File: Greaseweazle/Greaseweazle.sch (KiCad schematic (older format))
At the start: 16 parts, among them J1 FDC_PC, J2 PWR_EXT1, J3 PWR_DRV, J4 PWR_EXT2, J5 USB_TTL, J6 FDC_Amstrad, M1 Mounting, M2 Mounting, M3 Mounting, M4 Mounting

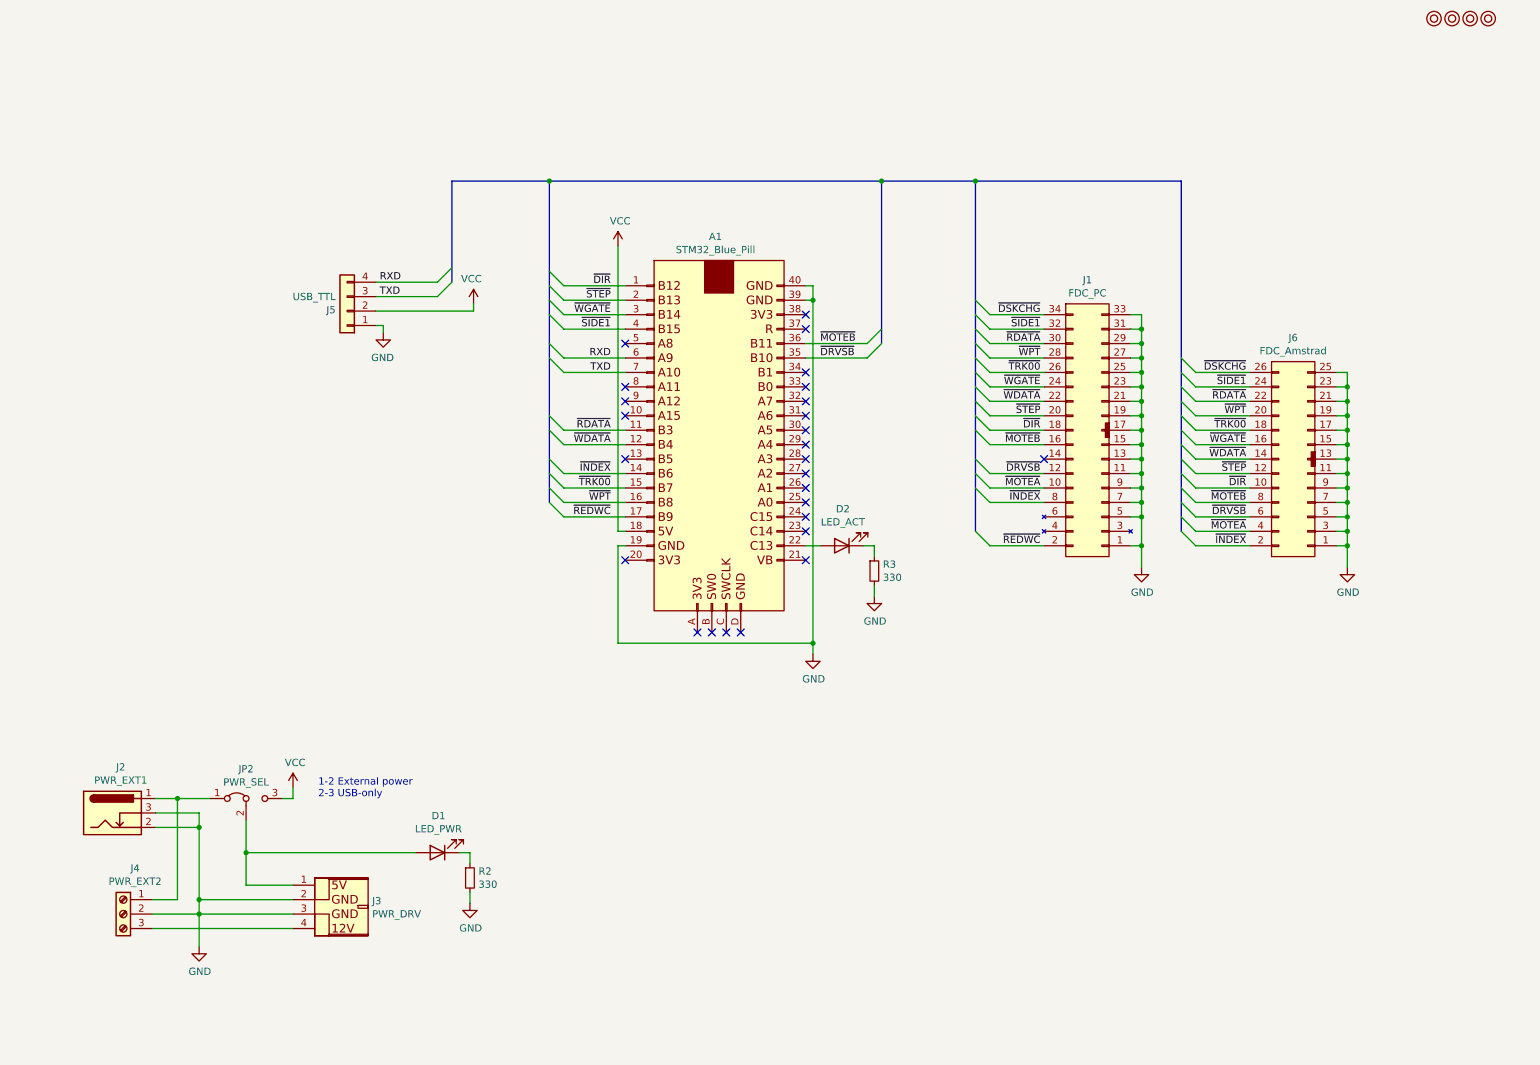
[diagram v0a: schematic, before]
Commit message: Invert activity LED
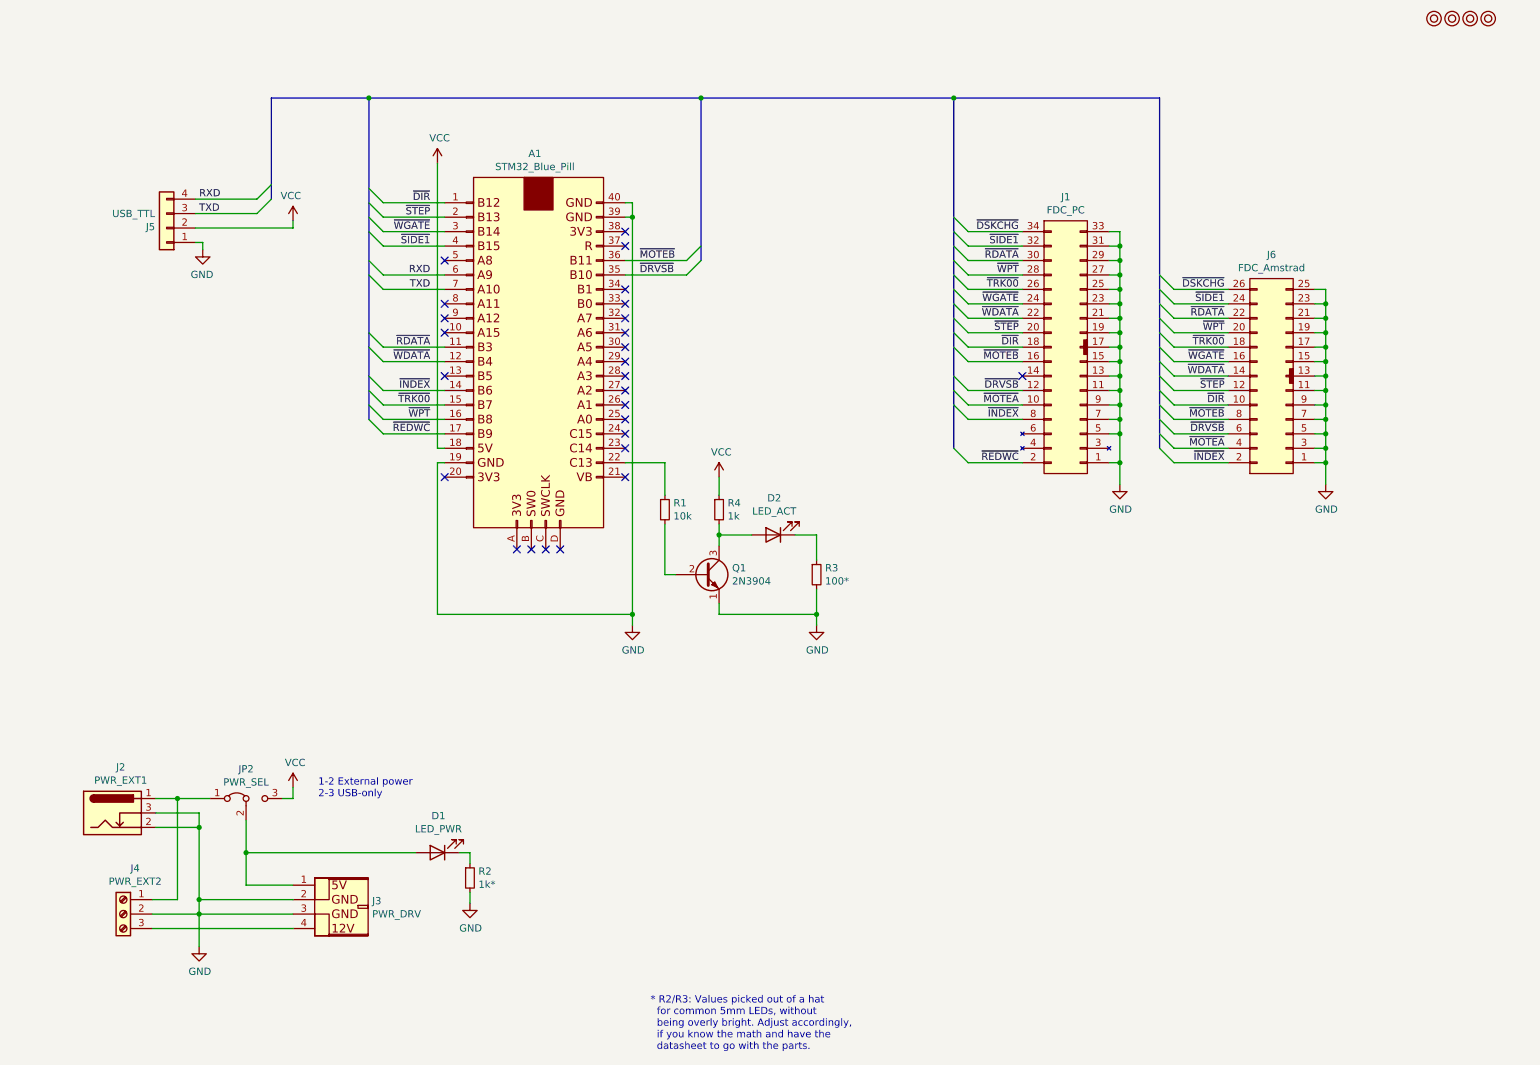
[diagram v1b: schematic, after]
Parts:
- added Q1: 2N3904, Package_TO_SOT_THT:TO-92_Inline_Wide, symbol Transistor_BJT:2N3904
- added R1: 10k, Resistor_THT:R_Axial_DIN0207_L6.3mm_D2.5mm_P10.16mm_Horizontal, symbol Device:R_Small
- added R4: 1k, Resistor_THT:R_Axial_DIN0207_L6.3mm_D2.5mm_P10.16mm_Horizontal, symbol Device:R_Small
- R2: value 330 -> 1k*
- R3: value 330 -> 100*
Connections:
- net GND: now also Q1.1 (E)
- net VCC: now also R4.1
- net at D2.2 (A): now also Q1.3 (C), R4.2; no longer A1.22 (C13)
- new net: A1.22 (C13), R1.1
- new net: Q1.2 (B), R1.2
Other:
- note added: "* R2/R3: Values picked out of a hat\n for common 5mm LEDs, without\n being overly bright. Adjust accordingly,\n if you know the math and have the\n datasheet to go with the parts."
- moved on the sheet: A1, D2, J1, J5, J6, R3

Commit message: Tweaked Amstrad pinout to match pins available (still untested)
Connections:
- net ~DRVSB: now also J6.4 (nc); no longer J6.6 (nc)
- net ~MOTEA: no longer names the net of J1.10 (/MOTEA)
- net ~MOTEA: no longer J6.4 (nc)
- no-connect marks 26 -> 28
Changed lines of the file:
@@
 Text Label 7875 3650 2    50   ~ 0
 ~REDWC
-NoConn ~ 7900 3050
 Entry Wire Line
 	7425 2050 7525 2150
@@
 Wire Wire Line
 	8950 3650 9325 3650
-Text Label 9300 3450 2    50   ~ 0
-~DRVSB
-Wire Wire Line
-	8950 3450 9325 3450
-Text Label 9300 3350 2    50   ~ 0
-~MOTEB
 Wire Wire Line
 	8950 3350 9325 3350
@@
 Entry Wire Line
 	8850 2350 8950 2450
-Text Label 7875 3250 2    50   ~ 0
-~MOTEA
-Wire Wire Line
-	7525 3250 7900 3250
-Text Label 9300 3550 2    50   ~ 0
-~MOTEA
 Wire Wire Line
 	8950 3550 9325 3550
-Entry Wire Line
-	8850 3350 8950 3450
-Entry Wire Line
-	7425 3150 7525 3250
 Wire Wire Line
 	2175 2025 2850 2025
@@
 Wire Bus Line
 	3375 1125 5675 1125
-Wire Bus Line
-	2700 1125 2700 1825
-Wire Bus Line
-	5675 1125 5675 2250
-Wire Bus Line
-	7425 1125 7425 3550
-Wire Bus Line
-	3375 1125 3375 3350
-Wire Bus Line
-	8850 1125 8850 3550
 Text Notes 5325 7725 0    50   ~ 0
 * R2/R3: Values picked out of a hat\n  for common 5mm LEDs, without\n  being overly bright. Adjust accordingly,\n  if you know the math and have the\n  datasheet to go with the parts.
+NoConn ~ 9325 3450
+NoConn ~ 7900 3050
+Text Label 9300 3350 2    50   ~ 0
+~MOTEB
+Text Label 9300 3550 2    50   ~ 0
+~DRVSB
+NoConn ~ 7900 3250
+Wire Bus Line
+	2700 1125 2700 1825
+Wire Bus Line
+	5675 1125 5675 2250
+Wire Bus Line
+	7425 1125 7425 3550
+Wire Bus Line
+	3375 1125 3375 3350
+Wire Bus Line
+	8850 1125 8850 3550
 $EndSCHEMATC

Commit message: Change PWR_EXT2 power input to 4pin
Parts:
- J4: footprint pwr_drv:PWR_EXT -> pwr_drv:PWR_IN; symbol Connector:Screw_Terminal_01x03 -> floppy:Power_Input
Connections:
- net GND: now also J4.3 (Pin_3)
- net at J2.1, JP2.1 (A): now also J4.4 (Pin_4); no longer J4.1 (Pin_1)
- net at J3.4 (Pin_4): now also J4.1 (Pin_1); no longer J4.3 (Pin_3)
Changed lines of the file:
@@
 L power:GND #PWR0108
 U 1 1 618BB95D
-P 2200 7000
-F 0 "#PWR0108" H 2200 6750 50  0001 C CNN
-F 1 "GND" H 2205 6827 50  0000 C CNN
-F 2 "" H 2200 7000 50  0001 C CNN
-F 3 "" H 2200 7000 50  0001 C CNN
-	1    2200 7000
+P 2150 7050
+F 0 "#PWR0108" H 2150 6800 50  0001 C CNN
+F 1 "GND" H 2155 6877 50  0000 C CNN
+F 2 "" H 2150 7050 50  0001 C CNN
+F 3 "" H 2150 7050 50  0001 C CNN
+	1    2150 7050
 	1    0    0    -1
 $EndComp
@@
 	1    0    0    -1
 $EndComp
-Wire Wire Line
-	2200 6675 2200 6175
-Connection ~ 2200 6675
-Wire Wire Line
-	2200 6075 2200 6175
-Connection ~ 2200 6175
 $Comp
 L Jumper:Jumper_3_Bridged12 JP2
@@
 1-2 External power\n2-3 USB-only
 Wire Wire Line
-	2200 6675 2200 6775
-Wire Wire Line
 	2525 6575 2850 6575
 Wire Wire Line
-	2200 6675 2850 6675
-Wire Wire Line
-	2850 6775 2200 6775
-Connection ~ 2200 6775
-Wire Wire Line
-	2200 6775 2200 7000
-$Comp
-L Connector:Screw_Terminal_01x03 J4
-U 1 1 61628176
-P 1675 6775
-F 0 "J4" H 1593 7092 50  0000 C CNN
-F 1 "PWR_EXT2" H 1593 7001 50  0000 C CNN
-F 2 "pwr_drv:PWR_EXT" H 1675 6775 50  0001 C CNN
-F 3 "~" H 1675 6775 50  0001 C CNN
-	1    1675 6775
-	-1   0    0    -1
-$EndComp
-Wire Wire Line
-	1875 6775 2200 6775
+	1875 6775 2150 6775
 Wire Wire Line
 	1900 5975 2050 5975
 Wire Wire Line
-	1900 6075 2200 6075
-Wire Wire Line
-	1900 6175 2200 6175
-Wire Wire Line
-	1875 6675 2050 6675
-Wire Wire Line
-	2050 6675 2050 5975
+	1900 6075 2150 6075
+Wire Wire Line
+	1900 6175 2150 6175
 Connection ~ 2050 5975
 Wire Wire Line
 	2050 5975 2275 5975
-Wire Wire Line
-	1875 6875 2850 6875
 $Comp
 L Device:LED D1
@@
 ~DRVSB
 NoConn ~ 7900 3250
+Wire Wire Line
+	1875 6575 2050 6575
+Wire Wire Line
+	2050 6575 2050 5975
+Wire Wire Line
+	1875 6875 2850 6875
+Wire Wire Line
+	1875 6675 2150 6675
+Wire Wire Line
+	2150 6075 2150 6175
+Connection ~ 2150 6175
+Wire Wire Line
+	2150 6175 2150 6675
+Connection ~ 2150 6675
+Wire Wire Line
+	2150 6675 2150 6775
+Connection ~ 2150 6775
+Wire Wire Line
+	2150 6775 2150 7050
+Wire Wire Line
+	2150 6775 2850 6775
+Wire Wire Line
+	2150 6675 2850 6675
+$Comp
+L floppy:Power_Input J4
+U 1 1 61628176
+P 1675 6775
+F 0 "J4" H 1675 7025 50  0000 C CNN
+F 1 "PWR_EXT2" H 1675 7100 50  0000 C CNN
+F 2 "pwr_drv:PWR_IN" H 1675 6775 50  0001 C CNN
+F 3 "~" H 1675 6775 50  0001 C CNN
+	1    1675 6775
+	-1   0    0    1
+$EndComp
 Wire Bus Line
 	2700 1125 2700 1825

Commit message: DKSCHG never actually connected to anything
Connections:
- net ~DSKCHG: no longer names the net of J1.34 (/DSKCHG)
- net ~DSKCHG: no longer J6.26 (/TRK00)
- no-connect marks 28 -> 30
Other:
- note added: "~DSKCHG"
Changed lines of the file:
@@
 NoConn ~ 5150 2150
 NoConn ~ 5150 2050
-$Comp
-L floppy:FDC_Amstrad J6
-U 1 1 6180066B
-P 9625 2850
-F 0 "J6" H 9625 3490 50  0000 C CNN
-F 1 "FDC_Amstrad" H 9625 3399 50  0000 C CNN
-F 2 "Connector_IDC:IDC-Header_2x13_P2.54mm_Vertical" H 9725 2700 50  0001 C CNN
-F 3 "~" H 9725 2700 50  0001 C CNN
-	1    9625 2850
-	1    0    0    -1
-$EndComp
-$Comp
-L power:GND #PWR0106
-U 1 1 618059FB
-P 10000 3800
-F 0 "#PWR0106" H 10000 3550 50  0001 C CNN
-F 1 "GND" H 10005 3627 50  0000 C CNN
-F 2 "" H 10000 3800 50  0001 C CNN
-F 3 "" H 10000 3800 50  0001 C CNN
-	1    10000 3800
-	1    0    0    -1
-$EndComp
-Wire Wire Line
-	10000 3800 10000 3650
-Wire Wire Line
-	10000 3650 9925 3650
-Wire Wire Line
-	10000 3650 10000 3550
-Wire Wire Line
-	10000 3450 9925 3450
-Connection ~ 10000 3650
-Wire Wire Line
-	9925 3350 10000 3350
-Wire Wire Line
-	10000 3350 10000 3450
-Connection ~ 10000 3450
-Wire Wire Line
-	9925 3250 10000 3250
-Wire Wire Line
-	10000 3250 10000 3350
-Connection ~ 10000 3350
-Wire Wire Line
-	9925 3150 10000 3150
-Wire Wire Line
-	10000 3150 10000 3250
-Connection ~ 10000 3250
-Wire Wire Line
-	9925 3050 10000 3050
-Wire Wire Line
-	10000 3050 10000 3150
-Connection ~ 10000 3150
-Wire Wire Line
-	9925 2950 10000 2950
-Wire Wire Line
-	10000 2950 10000 3050
-Connection ~ 10000 3050
-Wire Wire Line
-	9925 2850 10000 2850
-Wire Wire Line
-	10000 2850 10000 2950
-Connection ~ 10000 2950
-Wire Wire Line
-	9925 2750 10000 2750
-Wire Wire Line
-	10000 2750 10000 2850
-Connection ~ 10000 2850
-Wire Wire Line
-	10000 2750 10000 2650
-Wire Wire Line
-	10000 2650 9925 2650
-Connection ~ 10000 2750
-Wire Wire Line
-	10000 2650 10000 2550
-Wire Wire Line
-	10000 2550 9925 2550
-Connection ~ 10000 2650
-Wire Wire Line
-	10000 2550 10000 2450
-Wire Wire Line
-	10000 2450 9925 2450
-Connection ~ 10000 2550
-Text Label 9300 3650 2    50   ~ 0
-~INDEX
 Wire Wire Line
 	7525 3150 7900 3150
@@
 Wire Wire Line
 	7525 2150 7900 2150
-Wire Wire Line
-	8950 3650 9325 3650
-Wire Wire Line
-	8950 3350 9325 3350
-Text Label 9300 3250 2    50   ~ 0
-~DIR
-Wire Wire Line
-	8950 3250 9325 3250
-Text Label 9300 3150 2    50   ~ 0
-~STEP
-Wire Wire Line
-	8950 3150 9325 3150
-Text Label 9300 3050 2    50   ~ 0
-~WDATA
-Wire Wire Line
-	8950 3050 9325 3050
-Text Label 9300 2950 2    50   ~ 0
-~WGATE
-Wire Wire Line
-	8950 2950 9325 2950
-Text Label 9300 2850 2    50   ~ 0
-~TRK00
-Wire Wire Line
-	8950 2850 9325 2850
-Text Label 9300 2750 2    50   ~ 0
-~WPT
-Wire Wire Line
-	8950 2750 9325 2750
-Text Label 9300 2650 2    50   ~ 0
-~RDATA
-Wire Wire Line
-	8950 2650 9325 2650
-Text Label 9300 2550 2    50   ~ 0
-~SIDE1
-Wire Wire Line
-	8950 2550 9325 2550
-Wire Wire Line
-	9925 3550 10000 3550
-Connection ~ 10000 3550
-Wire Wire Line
-	10000 3550 10000 3450
-Entry Wire Line
-	8850 2450 8950 2550
-Entry Wire Line
-	8850 2550 8950 2650
-Entry Wire Line
-	8850 2650 8950 2750
-Entry Wire Line
-	8850 2750 8950 2850
-Entry Wire Line
-	8850 2850 8950 2950
-Entry Wire Line
-	8850 2950 8950 3050
-Entry Wire Line
-	8850 3050 8950 3150
-Entry Wire Line
-	8850 3150 8950 3250
-Entry Wire Line
-	8850 3250 8950 3350
-Entry Wire Line
-	8850 3450 8950 3550
-Entry Wire Line
-	8850 3550 8950 3650
 Wire Bus Line
 	8850 1125 7425 1125
 Connection ~ 7425 1125
-Text Label 7875 2050 2    50   ~ 0
-~DSKCHG
-Wire Wire Line
-	7900 2050 7525 2050
-Entry Wire Line
-	7425 1950 7525 2050
-Text Label 9300 2450 2    50   ~ 0
-~DSKCHG
-Wire Wire Line
-	9325 2450 8950 2450
-Entry Wire Line
-	8850 2350 8950 2450
-Wire Wire Line
-	8950 3550 9325 3550
 Wire Wire Line
 	2175 2025 2850 2025
@@
 Text Notes 5325 7725 0    50   ~ 0
 * R2/R3: Values picked out of a hat\n  for common 5mm LEDs, without\n  being overly bright. Adjust accordingly,\n  if you know the math and have the\n  datasheet to go with the parts.
-NoConn ~ 9325 3450
 NoConn ~ 7900 3050
-Text Label 9300 3350 2    50   ~ 0
-~MOTEB
-Text Label 9300 3550 2    50   ~ 0
-~DRVSB
 NoConn ~ 7900 3250
 Wire Wire Line
@@
 	-1   0    0    1
 $EndComp
+Text Label 9300 3550 2    50   ~ 0
+~DRVSB
+Text Label 9300 3350 2    50   ~ 0
+~MOTEB
+NoConn ~ 9325 3450
+Wire Wire Line
+	8950 3550 9325 3550
+Entry Wire Line
+	8850 3550 8950 3650
+Entry Wire Line
+	8850 3450 8950 3550
+Entry Wire Line
+	8850 3250 8950 3350
+Entry Wire Line
+	8850 3150 8950 3250
+Entry Wire Line
+	8850 3050 8950 3150
+Entry Wire Line
+	8850 2950 8950 3050
+Entry Wire Line
+	8850 2850 8950 2950
+Entry Wire Line
+	8850 2750 8950 2850
+Entry Wire Line
+	8850 2650 8950 2750
+Entry Wire Line
+	8850 2550 8950 2650
+Entry Wire Line
+	8850 2450 8950 2550
+Wire Wire Line
+	9925 3550 10000 3550
+Wire Wire Line
+	8950 2550 9325 2550
+Text Label 9300 2550 2    50   ~ 0
+~SIDE1
+Wire Wire Line
+	8950 2650 9325 2650
+Text Label 9300 2650 2    50   ~ 0
+~RDATA
+Wire Wire Line
+	8950 2750 9325 2750
+Text Label 9300 2750 2    50   ~ 0
+~WPT
+Wire Wire Line
+	8950 2850 9325 2850
+Text Label 9300 2850 2    50   ~ 0
+~TRK00
+Wire Wire Line
+	8950 2950 9325 2950
+Text Label 9300 2950 2    50   ~ 0
+~WGATE
+Wire Wire Line
+	8950 3050 9325 3050
+Text Label 9300 3050 2    50   ~ 0
+~WDATA
+Wire Wire Line
+	8950 3150 9325 3150
+Text Label 9300 3150 2    50   ~ 0
+~STEP
+Wire Wire Line
+	8950 3250 9325 3250
+Text Label 9300 3250 2    50   ~ 0
+~DIR
+Wire Wire Line
+	8950 3350 9325 3350
+Wire Wire Line
+	8950 3650 9325 3650
+Text Label 9300 3650 2    50   ~ 0
+~INDEX
+Wire Wire Line
+	10000 2450 9925 2450
+Wire Wire Line
+	10000 2550 10000 2450
+Connection ~ 10000 2550
+Wire Wire Line
+	10000 2550 9925 2550
+Wire Wire Line
+	10000 2650 10000 2550
+Connection ~ 10000 2650
+Wire Wire Line
+	10000 2650 9925 2650
+Wire Wire Line
+	10000 2750 10000 2650
+Connection ~ 10000 2750
+Wire Wire Line
+	9925 2750 10000 2750
+Wire Wire Line
+	10000 2750 10000 2850
+Connection ~ 10000 2850
+Wire Wire Line
+	9925 2850 10000 2850
+Wire Wire Line
+	10000 2850 10000 2950
+Connection ~ 10000 2950
+Wire Wire Line
+	9925 2950 10000 2950
+Wire Wire Line
+	10000 2950 10000 3050
+Connection ~ 10000 3050
+Wire Wire Line
+	9925 3050 10000 3050
+Wire Wire Line
+	10000 3050 10000 3150
+Connection ~ 10000 3150
+Wire Wire Line
+	9925 3150 10000 3150
+Wire Wire Line
+	10000 3150 10000 3250
+Connection ~ 10000 3250
+Wire Wire Line
+	9925 3250 10000 3250
+Wire Wire Line
+	10000 3250 10000 3350
+Connection ~ 10000 3350
+Wire Wire Line
+	9925 3350 10000 3350
+Wire Wire Line
+	10000 3550 10000 3450
+Wire Wire Line
+	10000 3350 10000 3450
+Connection ~ 10000 3450
+Wire Wire Line
+	10000 3450 9925 3450
+Connection ~ 10000 3550
+Wire Wire Line
+	10000 3650 10000 3550
+Wire Wire Line
+	10000 3650 9925 3650
+Connection ~ 10000 3650
+Wire Wire Line
+	10000 3800 10000 3650
+$Comp
+L power:GND #PWR0106
+U 1 1 618059FB
+P 10000 3800
+F 0 "#PWR0106" H 10000 3550 50  0001 C CNN
+F 1 "GND" H 10005 3627 50  0000 C CNN
+F 2 "" H 10000 3800 50  0001 C CNN
+F 3 "" H 10000 3800 50  0001 C CNN
+	1    10000 3800
+	1    0    0    -1
+$EndComp
+$Comp
+L floppy:FDC_Amstrad J6
+U 1 1 6180066B
+P 9625 2850
+F 0 "J6" H 9625 3490 50  0000 C CNN
+F 1 "FDC_Amstrad" H 9625 3399 50  0000 C CNN
+F 2 "Connector_IDC:IDC-Header_2x13_P2.54mm_Vertical" H 9725 2700 50  0001 C CNN
+F 3 "~" H 9725 2700 50  0001 C CNN
+	1    9625 2850
+	1    0    0    -1
+$EndComp
+NoConn ~ 7900 2050
 Wire Bus Line
 	2700 1125 2700 1825
@@
 Wire Bus Line
 	8850 1125 8850 3550
+NoConn ~ 9325 2450
+Text Notes 7875 2050 2    50   ~ 0
+~DSKCHG
 $EndSCHEMATC
